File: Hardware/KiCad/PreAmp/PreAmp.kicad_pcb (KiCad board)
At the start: 2 copper layers, 22 parts, among them J1 XLR3, J2 Conn_01x05_Pin, U1 TLV2371DBV, U2 INA217AIDWR

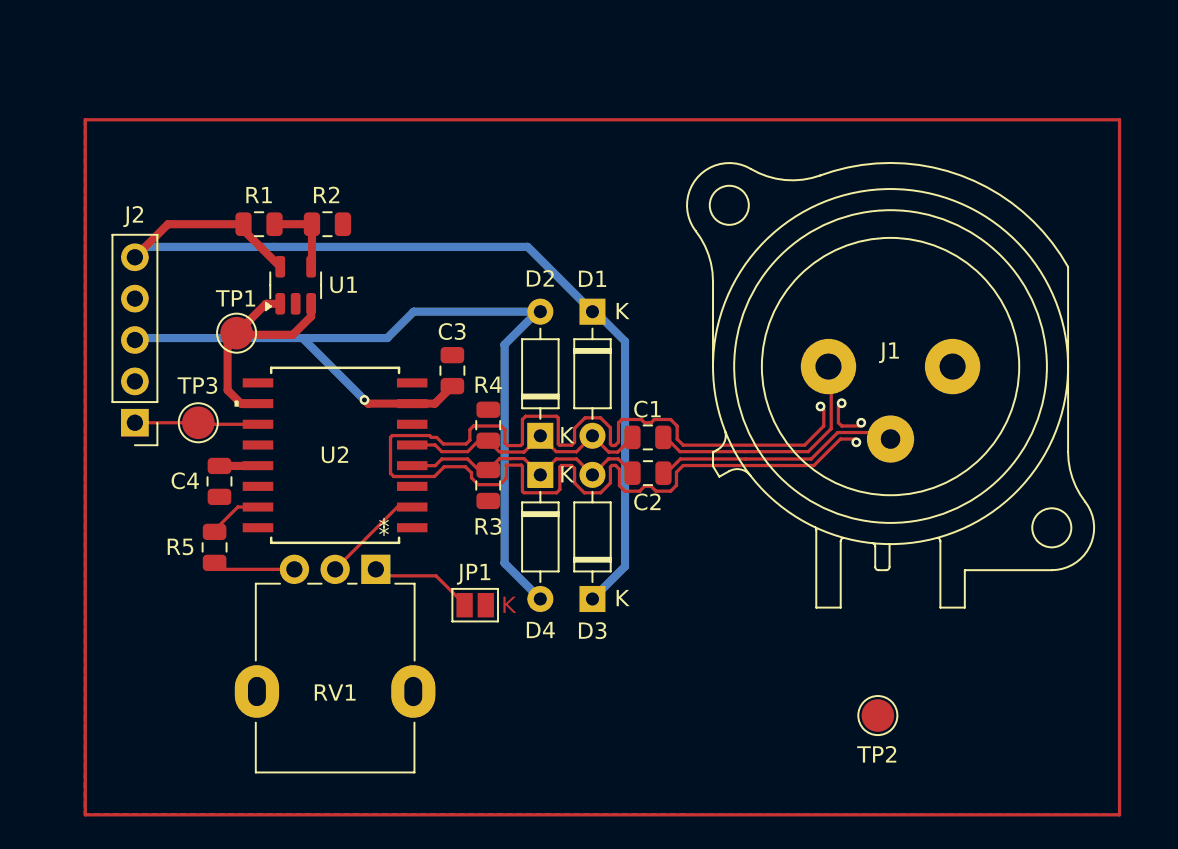
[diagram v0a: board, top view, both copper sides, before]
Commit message: Put back the 4 jumpers for possible improvement (reduce oscilation)
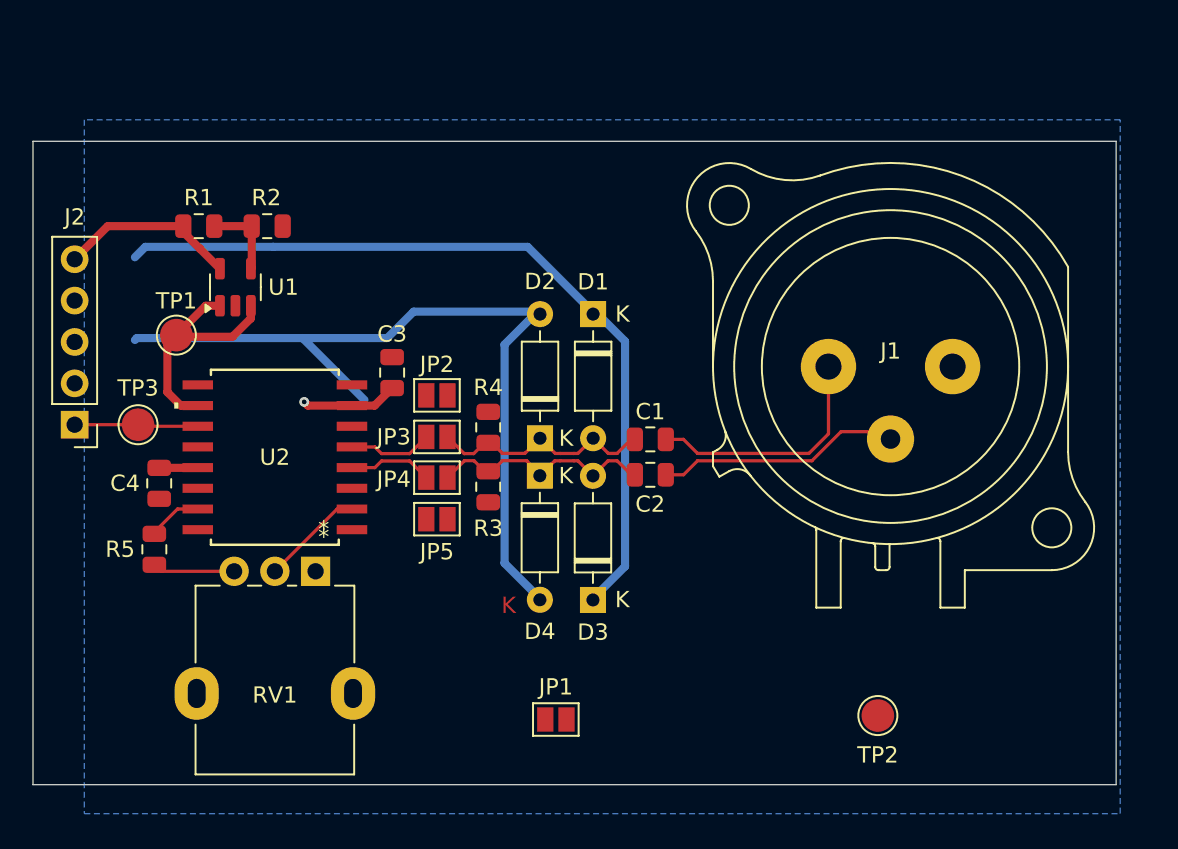
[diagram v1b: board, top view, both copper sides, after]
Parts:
- added JP2: SolderJumper_2_Open, Jumper:SolderJumper-2_P1.3mm_Open_Pad1.0x1.5mm, F.Cu at (140.1, 97.1)
- added JP3: SolderJumper_2_Open, Jumper:SolderJumper-2_P1.3mm_Open_Pad1.0x1.5mm, F.Cu at (140.1, 99.7)
- added JP4: SolderJumper_2_Open, Jumper:SolderJumper-2_P1.3mm_Open_Pad1.0x1.5mm, F.Cu at (140.1, 102.2)
- added JP5: SolderJumper_2_Open, Jumper:SolderJumper-2_P1.3mm_Open_Pad1.0x1.5mm, F.Cu at (140.1, 104.7)
- moved JP1 8.59 mm to (147.3, 117.0)
- moved R2 3.70 mm to (129.6, 86.7)
- moved RV1 3.70 mm to (132.6, 107.9)
- moved U2 3.70 mm to (130.1, 100.9)
- moved C4 3.70 mm to (123.0, 102.5)
- moved R5 3.70 mm to (122.7, 106.5)
- moved TP3 3.70 mm to (121.7, 98.9)
- moved C3 3.70 mm to (137.3, 95.7)
- moved J2 3.70 mm to (117.8, 98.9)
- moved R1 3.70 mm to (125.4, 86.7)
- moved TP1 3.70 mm to (124.1, 93.4)
- moved U1 3.70 mm to (127.7, 90.5)
- moved C1 0.19 mm to (153.2, 99.8)
- moved C2 0.17 mm to (153.2, 102.0)
- moved D1 0.16 mm to (149.6, 92.1)
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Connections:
- net /Input+ renamed /XLR+
- net /Input- renamed /XLR-
- C1 pad 2: /In+ -> /Cont+
- C2 pad 2: /In- -> /Cont-
- D1 pad 2: /In+ -> /Cont+
- D2 pad 1: /In+ -> /Cont+
- D3 pad 2: /In- -> /Cont-
- D4 pad 1: /In- -> /Cont-
- R3 pad 1: /In- -> /Cont-
- R4 pad 1: /In+ -> /Cont+
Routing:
- net GND: track 83.5 -> 0.00 mm, vias 4 -> 0
- net /Cont+: track 0.00 -> 14.7 mm
- net /Cont-: track 0.00 -> 14.4 mm
- net /In+: track 17.1 -> 5.16 mm
- net /In-: track 17.0 -> 5.16 mm
- net Net-(JP1-A): track 6.39 -> 0.00 mm
- removed copper zone on F.Cu, net GND
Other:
- board outline added: 66.5 x 39.5 mm

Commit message: Improved trough feedback Tijmen
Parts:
- moved JP1 11.1 mm to (138.4, 110.5)
- moved TP2 4.55 mm to (162.8, 115.5)
- moved R5 0.55 mm to (122.7, 106.0)
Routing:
- net 6V: track 62.9 -> 81.7 mm, vias 0 -> 2
- net Net-(JP1-A): track 0.00 -> 6.23 mm
- net -6V: track 56.7 -> 59.7 mm
- net /In+: track 5.16 -> 7.71 mm
- net /Cont+: track 14.7 -> 17.3 mm
- net /In-: track 5.16 -> 7.71 mm
- net /Cont-: track 14.4 -> 17.0 mm
- net GND: vias 0 -> 1
- added copper zone on F.Cu, net GND
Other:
- board size 66.5 x 39.5 mm -> 66.5 x 39.8 mm

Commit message: Included text on PCB
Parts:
- added H1: MountingHole_Pad, MountingHole:MountingHole_3.2mm_M3_DIN965_Pad_TopBottom, F.Cu at (178.0, 117.2)
- added H2: MountingHole_Pad, MountingHole:MountingHole_3.2mm_M3_DIN965_Pad_TopBottom, F.Cu at (119.0, 117.2)
- added H3: MountingHole_Pad, MountingHole:MountingHole_3.2mm_M3_DIN965_Pad_TopBottom, F.Cu at (119.0, 78.6)
- added H4: MountingHole_Pad, MountingHole:MountingHole_3.2mm_M3_DIN965_Pad_TopBottom, F.Cu at (178.0, 78.6)
- moved C4 0.61 mm to (122.4, 102.4), turned to 180 degrees
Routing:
- net GND: track 0.00 -> 2.37 mm, vias 1 -> 2
- net 6V: track 81.7 -> 82.4 mm
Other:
- board size 66.5 x 39.8 mm -> 66.5 x 46.2 mm
- board text added: "Microphone Preamp Module"
- board text added: "Sounds Like Tim"
- board text added: "rev 1"

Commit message: Generated files for production
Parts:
- C1, C2: footprint Capacitor_SMD:C_0805_2012Metric -> Capacitor_SMD:C_1206_3216Metric
- C3, C4: footprint Capacitor_SMD:C_0805_2012Metric -> Capacitor_Tantalum_SMD:CP_EIA-3216-18_Kemet-A
- moved H1 1.75 mm to (179.8, 117.2)
- moved H4 1.75 mm to (179.8, 78.6)
- moved J1 1.59 mm to (173.3, 95.3)
- moved C4 0.91 mm to (121.5, 102.5)
- moved C2 0.86 mm to (154.0, 102.1)
- moved C1 0.85 mm to (154.0, 99.8)
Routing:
- net 6V: track 82.4 -> 83.4 mm
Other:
- board size 66.5 x 46.2 mm -> 68.3 x 46.2 mm
- board text removed: "K"
